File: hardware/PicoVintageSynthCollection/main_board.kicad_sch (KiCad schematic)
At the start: 25 parts, among them J1 to front board, J2 to front board, J5 Bus 1 power/MIDI, J6 Bus 2 audio, J7 DEBUG UART0, U1 H11L1

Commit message: Lay out the main board, and find out what the module actually measures
The schematic said what connects to what. This says where it goes: 45 x 80 mm,
two layers, 630 track segments, ground poured on both sides, DRC clean and in
agreement with the schematic.

KiCad wants one board per project, so MainBoard/ is a second project whose root
sheet is a wrapper around the shared main_board.kicad_sch. There is one copy of
the schematic, not two -- every symbol now carries a second instance path, which
is the mechanism the file format has for exactly this. The nineteen
board-to-board signals end on global labels there, which is the truth: they
leave through J1 / J2 and continue on a board that does not exist yet.

The layout turned on one decision. With the RP2350-Plus on the front it stands
13.5 mm into the gap between the boards, and J1 / J2 would need long-pin headers
-- a part you have to go looking for. So everything sits on the back except the
two headers and eight 0805s, nothing between the boards is taller than a
capacitor, and ordinary headers reach. USB, the bus connectors and the module's
own BOOT and RESET buttons end up on the side you can reach with the module in a
case, and the USB-C lands at the board's top edge so a plug can come in from
above.

Four M2 standoff holes, which the document has been listing as missing since it
was written: the two header strips were the only mechanical link.

The PCM5102 module is the part of this that could have gone wrong quietly. Shops
list it as 32 x 24 mm and one careful blog says 29 x 16; it is neither. The STEP
model resolves to 31.8 x 17.3 with the two header rows 6.35 mm apart in one axis
and 0.635 in the other -- and 0.635 means they do not share a 2.54 grid, which
is not something anyone would guess. A KiCad footprint from a second source
agrees on both numbers to the micron. That is written down in
PCM5102_module_geometry.md, because it is the kind of fact that is expensive to
rediscover and invisible in the board 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
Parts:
- added H5, H6, H7, H8: M2 board standoff, MountingHole:MountingHole_2.2mm_M2, symbol Mechanical:MountingHole
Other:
- note added: "H5-H8: M2 standoffs to the front board, one per corner. The two header strips are not the only mechanical link."

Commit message: Give BOOT a spring pin so the module stays a plug-in part
BOOT was the only signal on either board that did not end on a connector
pin: it stopped at TP1, a solder pad, and a hand-soldered wire finished
the job at the module's underside. That works, but the sockets are in the
BOM specifically to keep the module replaceable, and a wire tethers it.

TP2 is a landing pad at 26.51 / 7.58, under the module's BOOT pad, for a
spring-loaded pin spanning 11.04 mm -- socket body 8.5 plus header plastic
2.54, both read out of their own STEP models. Seating the module makes the
contact. TP1 stays, out at the edge where an iron reaches, because two
things about that position are unsettled: the coordinate comes from the
Raspberry Pi Pico 2 datasheet and the module is a WeAct RP2350-Plus with
its own layout, and the sign of X depends on which side that drawing is
viewed from. Both are settled by looking at the part -- is the pad nearer
the GP0 row or the VBUS row -- and only that one number changes. If it
turns out to be somewhere else entirely, it is the short-wire build after
all and nothing is lost.

The pad landed on UART0_RX, so that net was laid again. The first attempt
then took the corridor past C9 and pinched the ground pour into an 8.4 mm²
island with C9's own ground pad inside it -- the RUN capacitor would have
had no return path. Too narrow for a stitching via (widest point 0.468 mm,
a 0.6 mm via needs 0.50), so the corridor is a router keep-out now and
UART0_RX goes round.

Both boards: 0 open DRC, 0 unconnected, 0 parity, ERC 0 on all three
schematics. One documented exclusion, for TP2's hole sitting inside A1's
courtyard -- that pair only, so the rule still guards the rest of the
board.

Co-Authored-By: Claude Opus 5 <noreply@anthropic.com>
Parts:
- added TP2: BOOT pogo, TestPoint:TestPoint_THTPad_D2.0mm_Drill1.0mm, symbol Connector:TestPoint
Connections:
- net BOOT: now also TP2.1
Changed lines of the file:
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@@
 		(pts
 			(xy 24.13 195.58)
-			(xy 36.83 195.58)
+			(xy 44.45 195.58)
+		)
+		(stroke
+			(width 0)
+			(type default)
+		)
+	)
+	(wire
+		(pts
+			(xy 44.45 195.58)
+			(xy 44.45 190.5)
 		)
 		(stroke
@@
 					(unit 1)
 				)
+			)
+		)
+	)
+	(symbol
+		(lib_id "Connector:TestPoint")
+		(at 44.45 190.5 0)
+		(unit 1)
+		(body_style 1)
+		(exclude_from_sim no)
+		(in_bom yes)
+		(on_board yes)
+		(in_pos_files yes)
+		(dnp no)
+		(property "Reference" "TP2"
+			(at 39.37 186.69 0)
+			(show_name no)
+			(do_not_autoplace no)
+			(effects
+				(font
+					(size 1.27 1.27)
+				)
+				(justify left)
+			)
+		)
+		(property "Value" "BOOT pogo"
+			(at 39.37 184.15 0)
+			(show_name no)
+			(do_not_autoplace no)
+			(effects
+				(font
+					(size 1.27 1.27)
+				)
+				(justify left)
+			)
+		)
+		(property "Footprint" "TestPoint:TestPoint_THTPad_D2.0mm_Drill1.0mm"
+			(at 44.45 190.5 0)
+			(show_name no)
+			(do_not_autoplace no)
+			(effects
+				(font
+					(size 1.27 1.27)
+				)
+				(hide yes)
+			)
+		)
+		(property "Datasheet" ""
+			(at 44.45 190.5 0)
+			(show_name no)
+			(do_not_autoplace no)
+			(effects
+				(font
+					(size 1.27 1.27)
+				)
+				(hide yes)
+			)
+		)
+		(property "Description" "Landing pad for a spring pin to the module BOOT pad, 11.04 mm above"
+			(at 44.45 190.5 0)
+			(show_name no)
+			(do_not_autoplace no)
+			(effects
+				(font
+					(size 1.27 1.27)
+				)
+				(hide yes)
+			)
+		)
+		(pin "1"
+		)
+		(instances
+			(project "PicoVintageSynthCollection"
+				(path "/717c5337-9c00-45ff-821b-4326af0f12e4/a1b2c3d4-0011-4a5b-8c6d-000000000012"
+					(reference "TP2")
+					(unit 1)
+				)
+			)
+			(project "MainBoard"
+				(path "/b2c3d4e5-0001-4a5b-8c6d-000000000101/b2c3d4e5-0011-4a5b-8c6d-000000000112"
+					(reference "TP2")
+					(unit 1)
+				)

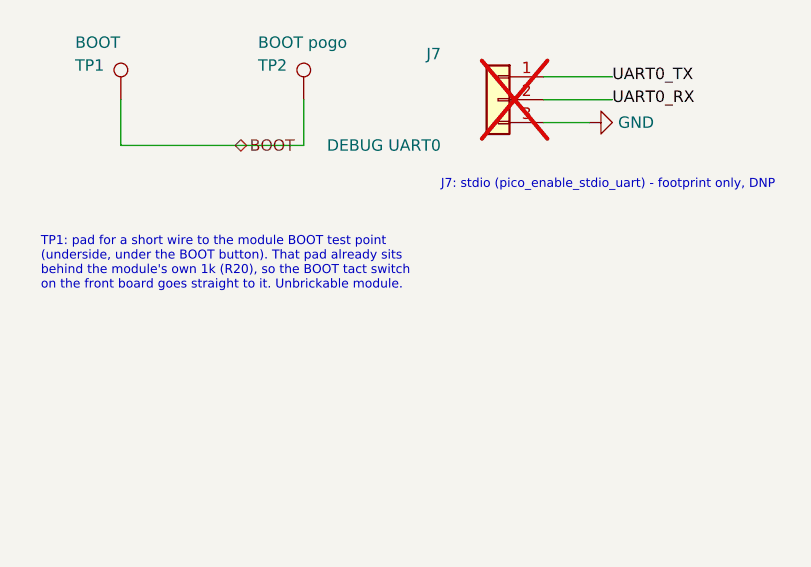
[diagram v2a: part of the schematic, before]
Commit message: The boards are drawn for a Pico 2, not for what I had written
Michael's correction: the target is a plain Raspberry Pi Pico 2, the
module most of the instruments here run on, and the Waveshare RP2350-Plus
is what goes in when 16 MB of flash is wanted. "WeAct" was my own
invention -- the top-level README has said Waveshare all along.

That flips the standing caveat on the spring pin. TP2's position comes
from the Pico 2 datasheet, so it is the drawn-for part's own document
rather than a number borrowed from a different board. Only the side of the
centreline was ever unsettled, because a drawing does not say which face
it is viewed from, and that is now checked on the part: nearer the GP0
row, which is the 26.51 already there.

What moves to the Waveshare board instead is the whole caveat: different
PCB, its BOOT pad is elsewhere, and that build uses TP1 and a wire. Which
is what TP1 is for. No board change to switch -- you fit either the pin or
the wire.

Also dropped a resistor designator that came from the wrong schematic, and
the note in the schematic now names TP6, TP2 and TP1 and says which build
takes which.

Co-Authored-By: Claude Opus 5 <noreply@anthropic.com>
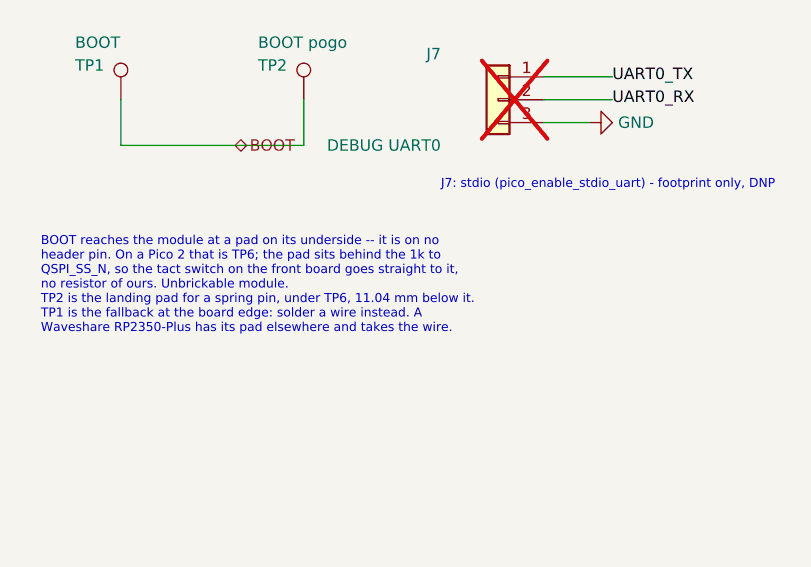
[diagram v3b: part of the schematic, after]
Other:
- note added: "BOOT reaches the module at a pad on its underside -- it is on no header pin. On a Pico 2 that is TP6; the pad sits behind the 1k to QSPI_SS_N, so the tact switch on the front board goes straight to it, no resistor of ours. Unbrickable module. TP2 is the landing pad for a spring pin, under TP6, 11.04 mm below it. TP1 is the fallback at the board edge: solder a wire instead. A Waveshare RP2350-Plus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"
- note removed: "TP1: pad for a short wire to the module BOOT test point (underside, under the BOOT button). That pad already sits behind the module's own 1k (R20), so the BOOT tact switch on the front board goes straight to it. Unbrickable module."
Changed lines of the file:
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@@
 		)
 	)
-	(text "TP1: pad for a short wire to the module BOOT test point\n(underside, under the BOOT button). That pad already sits\nbehind the module's own 1k (R20), so the BOOT tact switch\non the front board goes straight to it. Unbrickable module."
+	(text "BOOT reaches the module at a pad on its underside -- it is on no\nheader pin. On a Pico 2 that is TP6; the pad sits behind the 1k to\nQSPI_SS_N, so the tact switch on the front board goes straight to it,\nno resistor of ours. Unbrickable module.\nTP2 is the landing pad for a spring pin, under TP6, 11.04 mm below it.\nTP1 is the fallback at the board edge: solder a wire instead. A\nWaveshare RP2350-Plus has its pad elsewhere and takes the wire."
 		(exclude_from_sim no)
 		(at 15.24 205.74 0)
